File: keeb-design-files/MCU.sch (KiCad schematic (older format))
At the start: 36 parts, among them J1 Conn_ARM_JTAG_SWD_10, J2 SMA, J6 Conn_01x04, SW1 RESET, SW70 BOOT0, U1 STM32L452CEUx, U2 nRF24L01P, Y2 Crystal_GND24

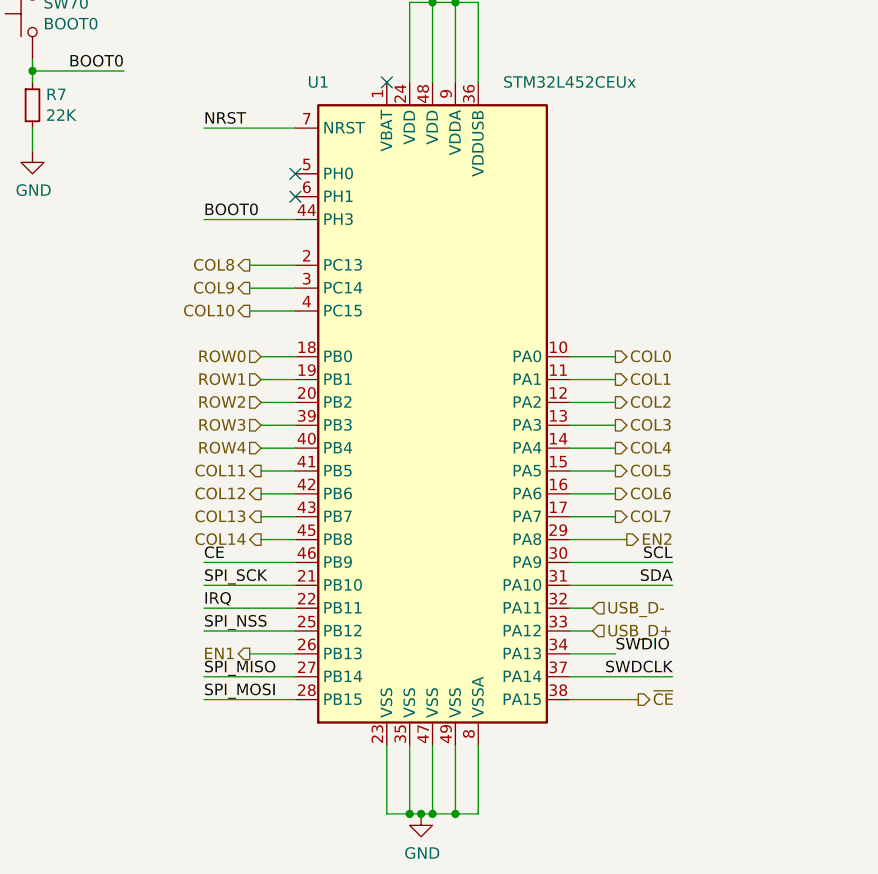
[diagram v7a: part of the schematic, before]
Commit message: Re-map MCU pins, Add LEDs, Remove USB Isolation cause it couldn't handle the POWER! More routing done
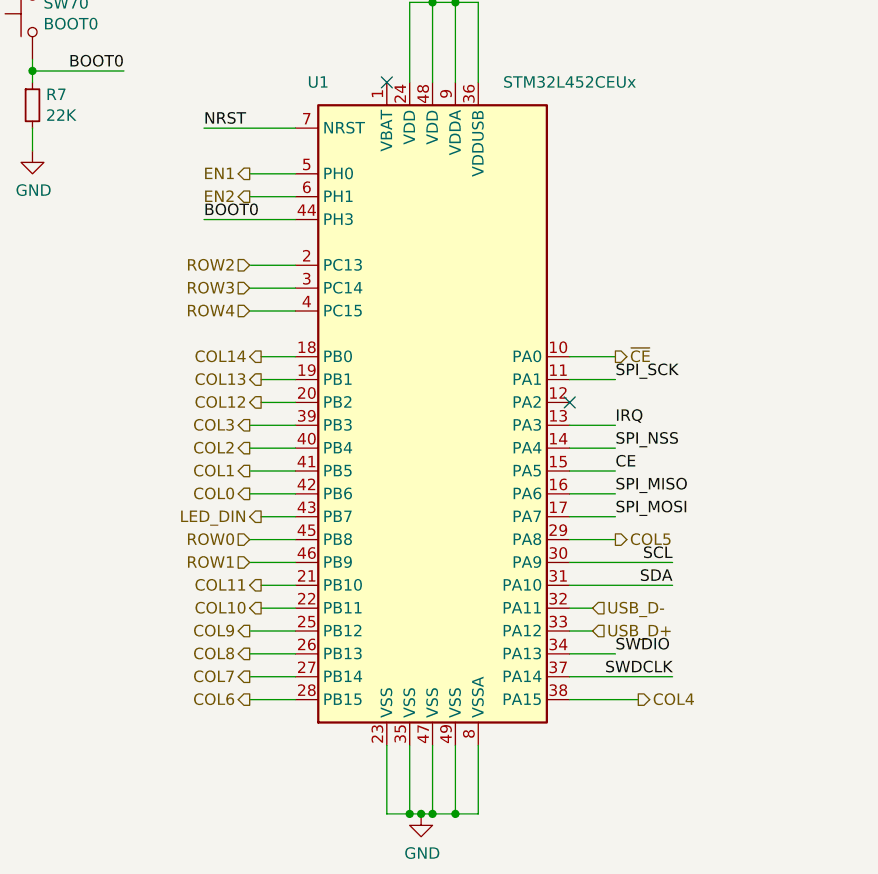
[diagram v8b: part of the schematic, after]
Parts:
- SW1, SW70: footprint Button_Switch_SMD:SW_SPST_B3S-1000 -> lib_fp:SW_SPST_B3S-1000
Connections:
- net CE: now also U1.15 (PA5); no longer U1.46 (PB9)
- net COL0: now also U1.42 (PB6); no longer U1.10 (PA0)
- net COL1: now also U1.41 (PB5); no longer U1.11 (PA1)
- net COL10: now also U1.22 (PB11); no longer U1.4 (PC15)
- net COL11: now also U1.21 (PB10); no longer U1.41 (PB5)
- net COL12: now also U1.20 (PB2); no longer U1.42 (PB6)
- net COL13: now also U1.19 (PB1); no longer U1.43 (PB7)
- net COL14: now also U1.18 (PB0); no longer U1.45 (PB8)
- net COL2: now also U1.40 (PB4); no longer U1.12 (PA2)
- net COL3: now also U1.39 (PB3); no longer U1.13 (PA3)
- net COL4: now also U1.38 (PA15); no longer U1.14 (PA4)
- net COL5: now also U1.29 (PA8); no longer U1.15 (PA5)
- net COL6: now also U1.28 (PB15); no longer U1.16 (PA6)
- net COL7: now also U1.27 (PB14); no longer U1.17 (PA7)
- net COL8: now also U1.26 (PB13); no longer U1.2 (PC13)
- net COL9: now also U1.25 (PB12); no longer U1.3 (PC14)
- net EN1: now also U1.5 (PH0); no longer U1.26 (PB13)
- net EN2: now also U1.6 (PH1); no longer U1.29 (PA8)
- net IRQ: now also U1.13 (PA3); no longer U1.22 (PB11)
- net ROW0: now also U1.45 (PB8); no longer U1.18 (PB0)
- net ROW1: now also U1.46 (PB9); no longer U1.19 (PB1)
- net ROW2: now also U1.2 (PC13); no longer U1.20 (PB2)
- net ROW3: now also U1.3 (PC14); no longer U1.39 (PB3)
- net ROW4: now also U1.4 (PC15); no longer U1.40 (PB4)
- net SPI_MISO: now also U1.16 (PA6); no longer U1.27 (PB14)
- net SPI_MOSI: now also U1.17 (PA7); no longer U1.28 (PB15)
- net SPI_NSS: now also U1.14 (PA4); no longer U1.25 (PB12)
- net SPI_SCK: now also U1.11 (PA1); no longer U1.21 (PB10)
- net ~CE~: now also U1.10 (PA0); no longer U1.38 (PA15)
- new net LED_DIN: U1.43 (PB7)
- no-connect marks 6 -> 5
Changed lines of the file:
@@
 	1    0    0    -1
 $EndComp
-Text Label 3450 3850 0    50   ~ 0
+Text Label 5250 3050 0    50   ~ 0
 SPI_NSS
-Text Label 3450 3650 0    50   ~ 0
+Text Label 5250 2750 0    50   ~ 0
 SPI_SCK
 Wire Wire Line
-	3450 3850 3850 3850
-Wire Wire Line
-	3850 4050 3450 4050
+	3650 3850 3850 3850
+Wire Wire Line
+	3850 4050 3650 4050
 Text Label 7300 1800 0    50   ~ 0
 SPI_SCK
@@
 	5050 3850 5150 3850
 Wire Wire Line
-	3850 3650 3450 3650
-Wire Wire Line
-	3850 4150 3450 4150
-Text Label 3450 4150 0    50   ~ 0
+	3850 3650 3700 3650
+Wire Wire Line
+	3850 4150 3650 4150
+Text Label 5250 3350 0    50   ~ 0
 SPI_MOSI
 $Comp
@@
 Text Label 7550 2100 2    50   ~ 0
 CE
-Text Label 3450 3550 0    50   ~ 0
+Text Label 5250 3150 0    50   ~ 0
 CE
 Wire Wire Line
-	3450 3550 3850 3550
-Text Label 3450 3750 0    50   ~ 0
+	3650 3550 3850 3550
+Text Label 5250 2950 0    50   ~ 0
 IRQ
 Wire Wire Line
-	3450 3750 3850 3750
+	3700 3750 3850 3750
 $Comp
 L Connector:Conn_ARM_JTAG_SWD_10 J1
@@
 Wire Wire Line
 	9150 2450 9150 2500
-Text HLabel 3700 2650 0    50   Input ~ 0
+Text HLabel 3650 3450 0    50   Input ~ 0
 ROW0
-Text HLabel 3700 2750 0    50   Input ~ 0
+Text HLabel 3650 3550 0    50   Input ~ 0
 ROW1
-Text HLabel 3700 2850 0    50   Input ~ 0
+Text HLabel 3650 2250 0    50   Input ~ 0
 ROW2
-Text HLabel 3700 2950 0    50   Input ~ 0
+Text HLabel 3650 2350 0    50   Input ~ 0
 ROW3
-Text HLabel 3700 3050 0    50   Input ~ 0
+Text HLabel 3650 2450 0    50   Input ~ 0
 ROW4
-Text HLabel 5250 2650 2    50   Output ~ 0
+Text HLabel 3650 3250 0    50   Output ~ 0
 COL0
-Text HLabel 5250 2750 2    50   Output ~ 0
+Text HLabel 3650 3150 0    50   Output ~ 0
 COL1
-Text HLabel 5250 2850 2    50   Output ~ 0
+Text HLabel 3650 3050 0    50   Output ~ 0
 COL2
-Text HLabel 5250 2950 2    50   Output ~ 0
+Text HLabel 3650 2950 0    50   Output ~ 0
 COL3
-Text HLabel 5250 3050 2    50   Output ~ 0
+Text HLabel 5350 4150 2    50   Output ~ 0
 COL4
-Text HLabel 5250 3150 2    50   Output ~ 0
+Text HLabel 5250 3450 2    50   Output ~ 0
 COL5
-Text HLabel 5250 3250 2    50   Output ~ 0
+Text HLabel 3650 4150 0    50   Output ~ 0
 COL6
-Text HLabel 5250 3350 2    50   Output ~ 0
+Text HLabel 3650 4050 0    50   Output ~ 0
 COL7
-Text HLabel 3650 2250 0    50   Output ~ 0
+Text HLabel 3650 3950 0    50   Output ~ 0
 COL8
-Text HLabel 3650 2350 0    50   Output ~ 0
+Text HLabel 3650 3850 0    50   Output ~ 0
 COL9
-Text HLabel 3650 2450 0    50   Output ~ 0
+Text HLabel 3700 3750 0    50   Output ~ 0
 COL10
-Text HLabel 3700 3150 0    50   Output ~ 0
+Text HLabel 3700 3650 0    50   Output ~ 0
 COL11
-Text HLabel 3700 3250 0    50   Output ~ 0
+Text HLabel 3700 2850 0    50   Output ~ 0
 COL12
-Text HLabel 3700 3350 0    50   Output ~ 0
+Text HLabel 3700 2750 0    50   Output ~ 0
 COL13
-Text HLabel 3700 3450 0    50   Output ~ 0
+Text HLabel 3700 2650 0    50   Output ~ 0
 COL14
 Wire Wire Line
@@
 	5050 2750 5250 2750
 Wire Wire Line
-	5050 2850 5250 2850
-Wire Wire Line
 	5050 2950 5250 2950
 Wire Wire Line
@@
 	3850 2450 3650 2450
 Wire Wire Line
-	3850 3150 3700 3150
-Wire Wire Line
-	3850 3250 3700 3250
+	3850 3150 3650 3150
+Wire Wire Line
+	3850 3250 3650 3250
 Wire Wire Line
 	3850 3350 3700 3350
 Wire Wire Line
-	3850 3450 3700 3450
+	3850 3450 3650 3450
 Wire Wire Line
 	3700 2650 3850 2650
@@
 	3850 2850 3700 2850
 Wire Wire Line
-	3850 2950 3700 2950
-Wire Wire Line
-	3850 3050 3700 3050
+	3850 2950 3650 2950
+Wire Wire Line
+	3850 3050 3650 3050
 Wire Notes Line width 20
 	11100 700  6950 700
@@
 F 0 "SW1" V 1096 1402 50  0000 R CNN
 F 1 "RESET" V 1005 1402 50  0000 R CNN
-F 2 "Button_Switch_SMD:SW_SPST_B3S-1000" H 1050 1650 50  0001 C CNN
+F 2 "lib_fp:SW_SPST_B3S-1000" H 1050 1650 50  0001 C CNN
 F 3 "~" H 1050 1650 50  0001 C CNN
 	1    1050 1450
@@
 	3450 1650 3850 1650
 NoConn ~ 4250 1450
-Text Label 3450 4050 0    50   ~ 0
+Text Label 5250 3250 0    50   ~ 0
 SPI_MISO
 NoConn ~ 3100 6300
@@
 F 0 "SW70" V 2746 1102 50  0000 R CNN
 F 1 "BOOT0" V 2655 1102 50  0000 R CNN
-F 2 "Button_Switch_SMD:SW_SPST_B3S-1000" H 2700 1350 50  0001 C CNN
+F 2 "lib_fp:SW_SPST_B3S-1000" H 2700 1350 50  0001 C CNN
 F 3 "~" H 2700 1350 50  0001 C CNN
 	1    2700 1150
@@
 Wire Wire Line
 	2700 1400 2700 1350
-NoConn ~ 3850 1850
-NoConn ~ 3850 1950
 Wire Wire Line
 	5350 4150 5050 4150
-Text HLabel 5350 4150 2    50   Output ~ 0
+Text HLabel 5250 2650 2    50   Output ~ 0
 ~CE~
-Text HLabel 3650 3950 0    50   Output ~ 0
+Text HLabel 3650 1850 0    50   Output ~ 0
 EN1
-Text HLabel 5300 3450 2    50   Output ~ 0
+Text HLabel 3650 1950 0    50   Output ~ 0
 EN2
 $Comp
@@
 	5050 3650 5500 3650
 Wire Wire Line
-	5050 3450 5300 3450
-Wire Wire Line
-	3650 3950 3850 3950
+	5050 3450 5250 3450
 Text Notes 10100 6350 0    50   ~ 10
 OLED Display Connector
@@
 Text Notes 8550 6350 0    50   ~ 10
 I2C Pull-up Resistors
+Wire Wire Line
+	3650 1850 3850 1850
+Wire Wire Line
+	3650 1950 3850 1950
+Text HLabel 3700 3350 0    50   Output ~ 0
+LED_DIN
+Wire Wire Line
+	3650 3950 3850 3950
+NoConn ~ 5050 2850
 $EndSCHEMATC
